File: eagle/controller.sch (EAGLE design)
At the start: 1 part, among them X1 FH12-18S-0.5SH

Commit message: schematics added
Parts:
- added IC1, IC2: ULN2003AD, uln-udn:ULN2003AD
- added JP1: (no value), pinhead:PINHD-1X7/90
- added JP2, JP3, JP4: (no value), pinhead:PINHD-1X2
- added JP5: (no value), pinhead:PINHD-1X5/90
- added U1: ARDUINO_PRO_MINI, Halley.rpt:ARDUINO_PRO_MINI
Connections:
- new net GND: IC1.GND, IC2.GND, JP2.1, JP3.1, JP4.1, JP5.1, U1.GND
- new net N$1: IC1.I1, U1.A0
- new net N$10: IC2.I3, U1.D10
- new net N$11: IC2.I4, U1.D11(MOSI)
- new net N$12: IC2.I5, U1.D12(MISO)
- new net N$13: JP5.5, U1.D4
- new net N$14: JP5.4, U1.D5
- new net N$15: JP5.3, U1.D6
- new net N$16: JP5.2, U1.D7
- new net N$17: JP3.2, U1.TXO(D0)
- new net N$18: JP2.2, U1.RXI(D1)
- new net N$19: IC2.I6, U1.A5
- new net N$2: IC1.I2, U1.A1
- new net N$20: IC1.O1, JP1.1
- new net N$21: IC1.O2, JP1.2
- new net N$22: IC1.O3, JP1.3
- new net N$23: IC1.O4, JP1.4
- new net N$24: IC1.O5, JP1.5
- new net N$25: IC1.O6, JP1.6
- new net N$26: IC1.O7, JP1.7
- new net N$3: IC1.I3, U1.A2
- new net N$4: IC1.I4, U1.A3
- new net N$5: IC1.I5, U1.D3
- new net N$6: IC1.I6, U1.A4
- new net N$7: IC1.I7, U1.D2
- new net N$8: IC2.I1, U1.D8
- new net N$9: IC2.I2, U1.D9
- new net V+: JP4.2, U1.RAW
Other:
- moved on the sheet: X1-1, X1-10, X1-11, X1-12, X1-13, X1-14, X1-15, X1-16, X1-17, X1-18, X1-2, X1-3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

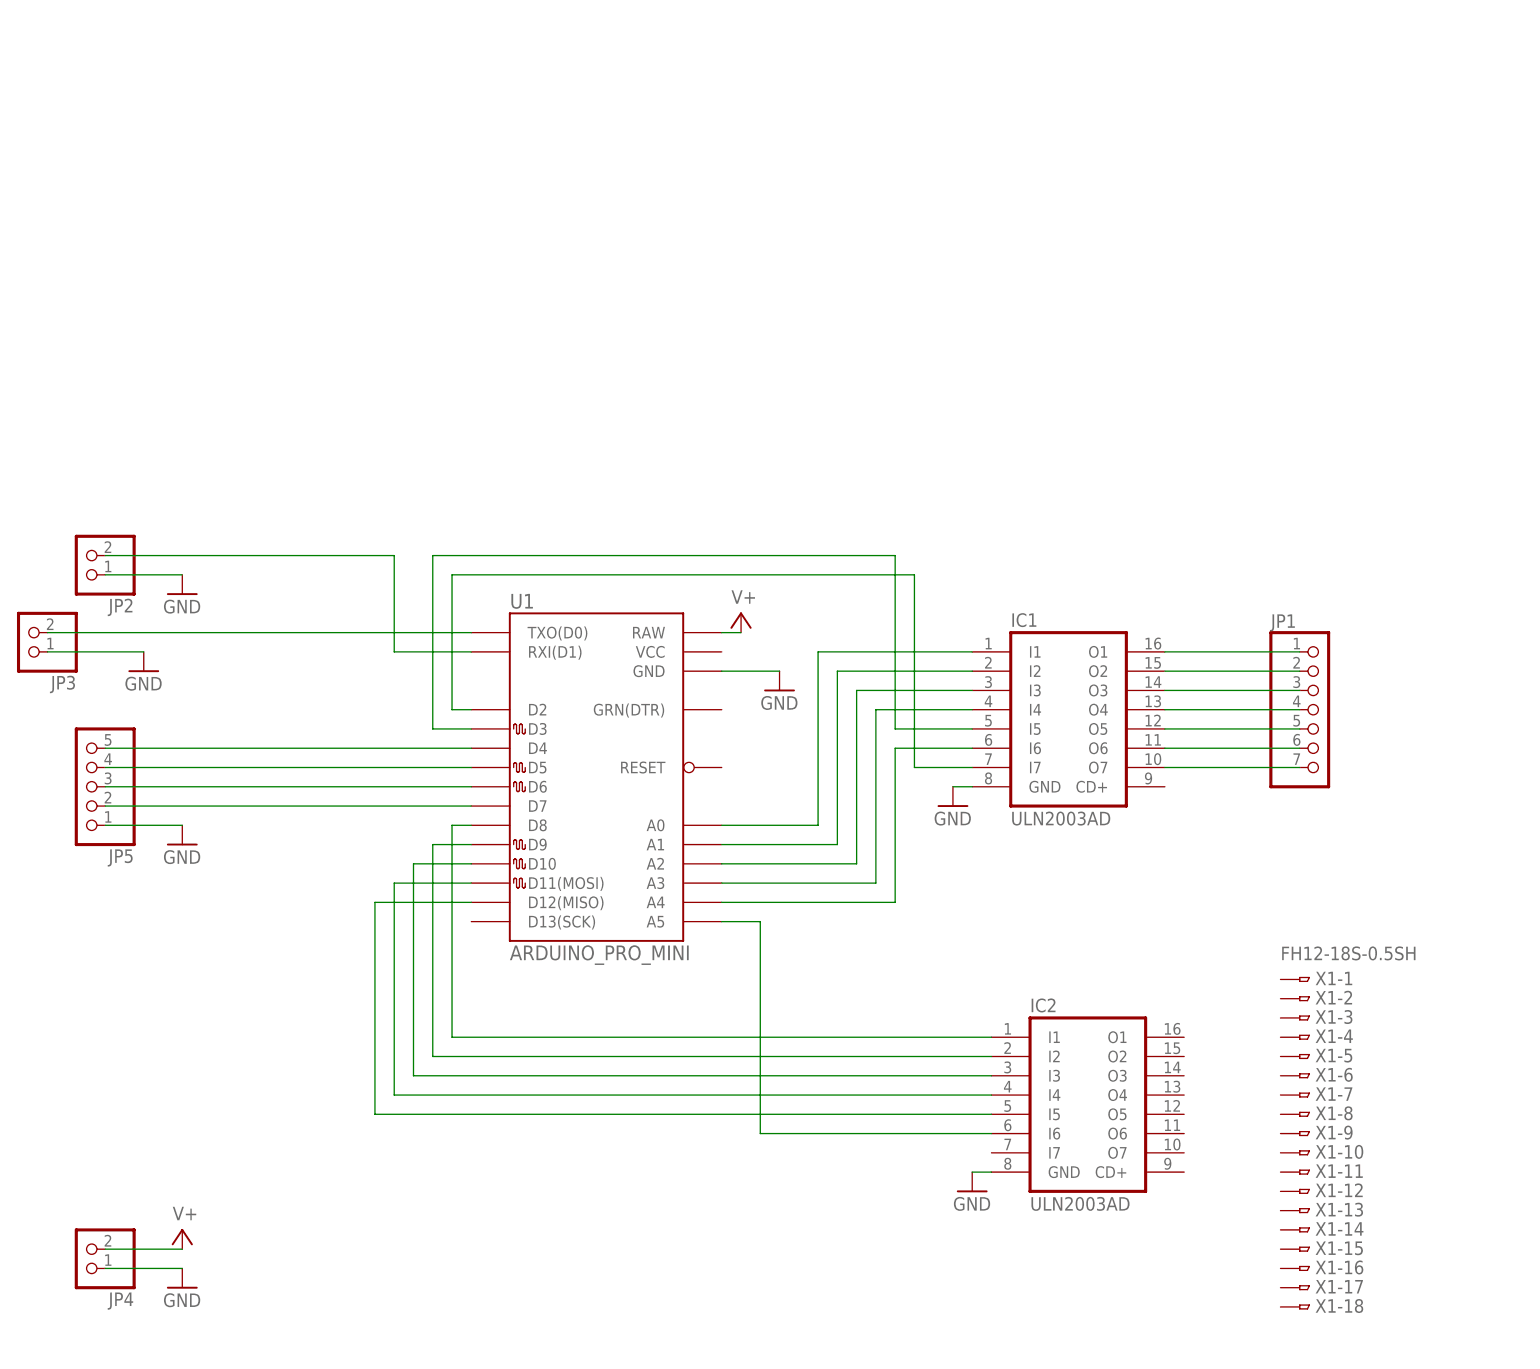
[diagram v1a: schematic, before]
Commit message: routed the board, updated bom
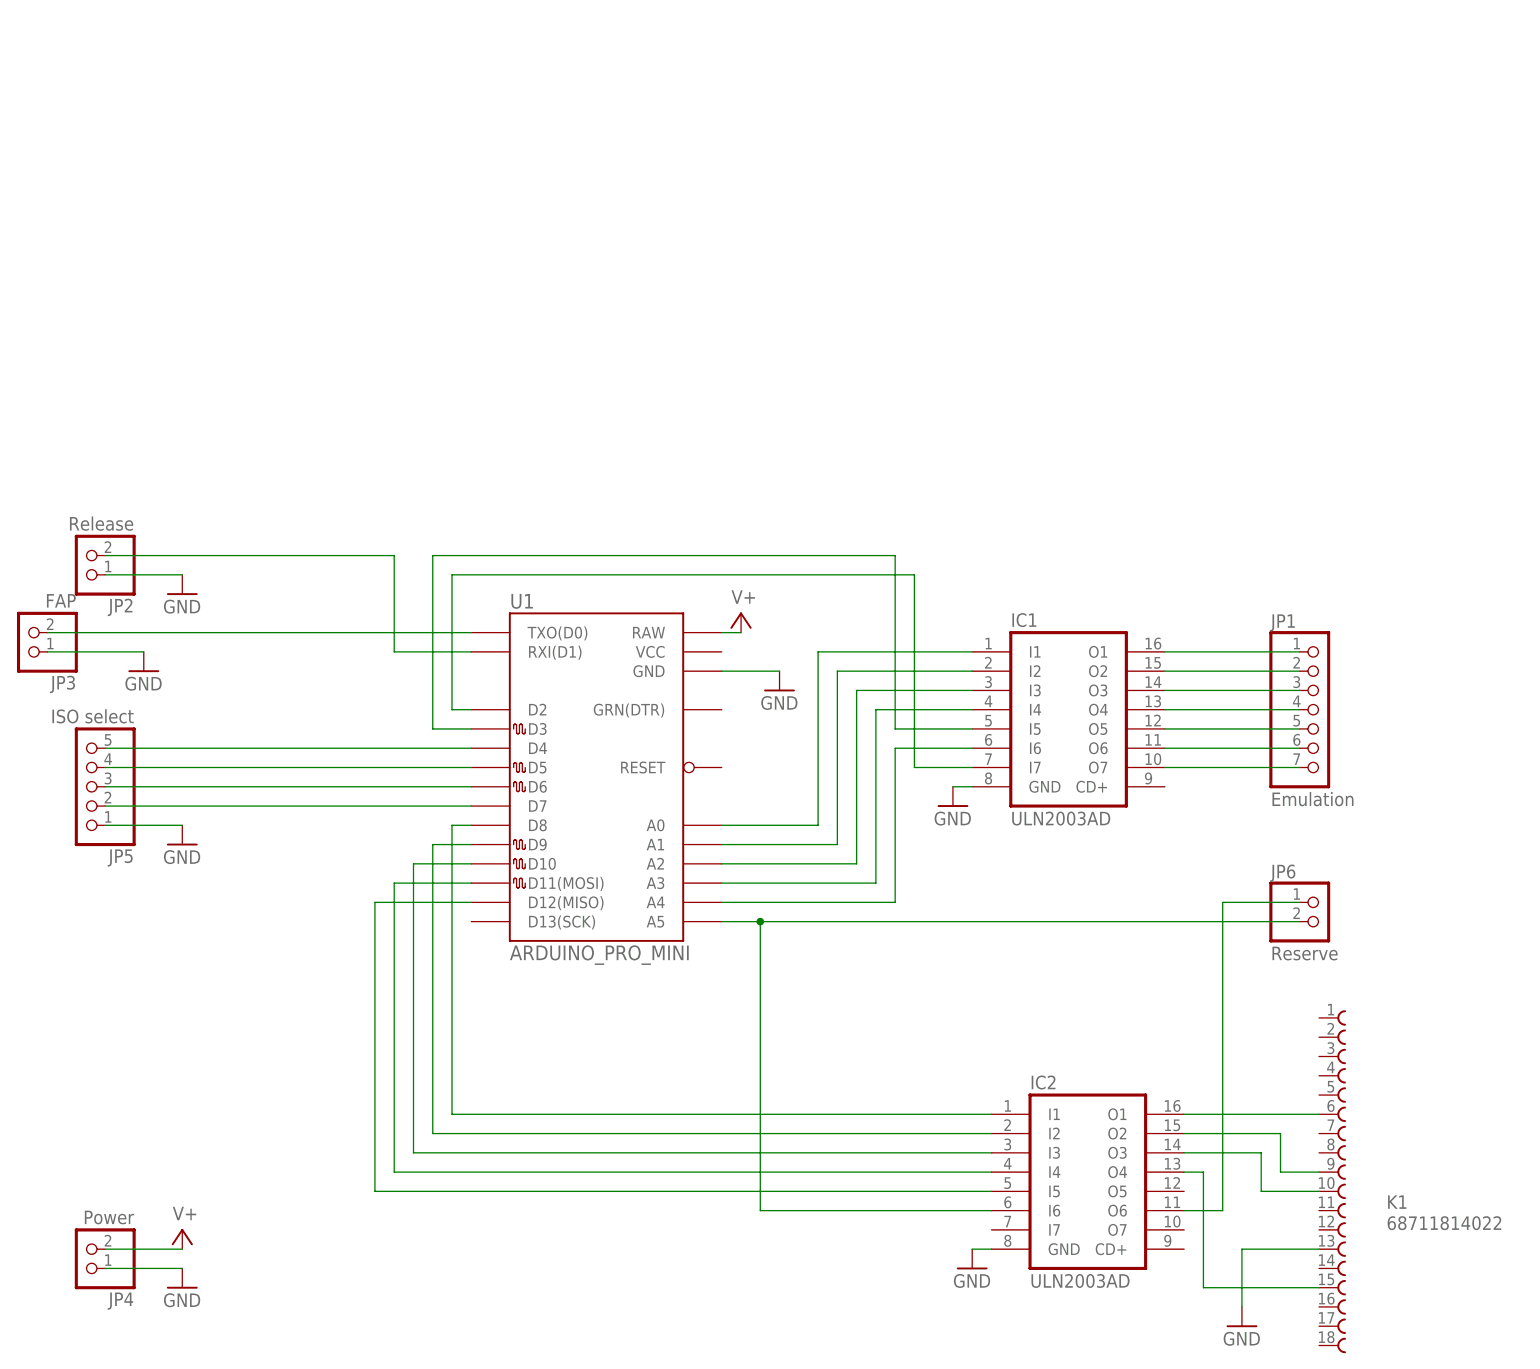
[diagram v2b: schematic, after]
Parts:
- removed X1: FH12-18S-0.5SH, con-hirose:FH12-18S-0.5SH
- added JP6: Reserve, pinhead:PINHD-1X2
- added K1: 68711814022, Wuerth_Elektronik_eiCan_03_ZIF_Connectors_Flat_Flexible_Cable:68711814022
- JP1: value (none) -> Emulation
- JP2: value (none) -> Release
- JP3: value (none) -> FAP
- JP4: value (none) -> Power
- JP5: value (none) -> ISO select
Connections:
- new net N$27: IC2.O6, JP6.1
- new net N$28: IC2.O1, K1.6
- new net N$29: IC2.O2, K1.9
- new net N$30: IC2.O3, K1.10
- new net N$31: IC2.O4, K1.15
- net GND: now also K1.13
- net N$19: now also JP6.2
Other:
- moved on the sheet: IC2
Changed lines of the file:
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@@
 </variantdefs>
 <classes>
-<class number="0" name="default" width="0" drill="0">
+<class number="0" name="default" width="0.2794" drill="0.381">
+<clearance class="0" value="0.1524"/>
 </class>
 </classes>
@@
 <part name="IC1" library="uln-udn" deviceset="ULN2003A" device="D"/>
 <part name="IC2" library="uln-udn" deviceset="ULN2003A" device="D"/>
-<part name="X1" library="con-hirose" deviceset="FH12-18S-0.5S" device="H"/>
 <part name="U1" library="Halley.rpt" deviceset="ARDUINO_PRO_MINI" device=""/>
 <part name="GND2" library="supply1" deviceset="GND" device=""/>
@@
 <part name="GND7" library="supply1" deviceset="GND" device=""/>
 <part name="GND1" library="supply1" deviceset="GND" device=""/>
-<part name="JP1" library="pinhead" deviceset="PINHD-1X7" device="/90"/>
-<part name="JP2" library="pinhead" deviceset="PINHD-1X2" device=""/>
-<part name="JP3" library="pinhead" deviceset="PINHD-1X2" device=""/>
-<part name="JP4" library="pinhead" deviceset="PINHD-1X2" device=""/>
-<part name="JP5" library="pinhead" deviceset="PINHD-1X5" device="/90"/>
+<part name="JP1" library="pinhead" deviceset="PINHD-1X7" device="/90" value="Emulation"/>
+<part name="JP2" library="pinhead" deviceset="PINHD-1X2" device="" value="Release"/>
+<part name="JP3" library="pinhead" deviceset="PINHD-1X2" device="" value="FAP"/>
+<part name="JP4" library="pinhead" deviceset="PINHD-1X2" device="" value="Power"/>
+<part name="JP5" library="pinhead" deviceset="PINHD-1X5" device="/90" value="ISO select"/>
+<part name="K1" library="Wuerth_Elektronik_eiCan_03_ZIF_Connectors_Flat_Flexible_Cable" deviceset="68711814022" device=""/>
+<part name="JP6" library="pinhead" deviceset="PINHD-1X2" device="" value="Reserve"/>
+<part name="GND8" library="supply1" deviceset="GND" device=""/>
 </parts>
 <sheets>
@@
 <instances>
 <instance part="IC1" gate="A" x="116.84" y="73.66"/>
-<instance part="IC2" gate="A" x="119.38" y="22.86"/>
-<instance part="X1" gate="-1" x="147.32" y="38.1"/>
-<instance part="X1" gate="-2" x="147.32" y="35.56"/>
-<instance part="X1" gate="-3" x="147.32" y="33.02"/>
-<instance part="X1" gate="-4" x="147.32" y="30.48"/>
-<instance part="X1" gate="-5" x="147.32" y="27.94"/>
-<instance part="X1" gate="-6" x="147.32" y="25.4"/>
-<instance part="X1" gate="-7" x="147.32" y="22.86"/>
-<instance part="X1" gate="-8" x="147.32" y="20.32"/>
-<instance part="X1" gate="-9" x="147.32" y="17.78"/>
-<instance part="X1" gate="-10" x="147.32" y="15.24"/>
-<instance part="X1" gate="-11" x="147.32" y="12.7"/>
-<instance part="X1" gate="-12" x="147.32" y="10.16"/>
-<instance part="X1" gate="-13" x="147.32" y="7.62"/>
-<instance part="X1" gate="-14" x="147.32" y="5.08"/>
-<instance part="X1" gate="-15" x="147.32" y="2.54"/>
-<instance part="X1" gate="-16" x="147.32" y="0"/>
-<instance part="X1" gate="-17" x="147.32" y="-2.54"/>
-<instance part="X1" gate="-18" x="147.32" y="-5.08"/>
+<instance part="IC2" gate="A" x="119.38" y="12.7"/>
 <instance part="U1" gate="G$1" x="53.34" y="63.5"/>
-<instance part="GND2" gate="1" x="104.14" y="10.16"/>
+<instance part="GND2" gate="1" x="104.14" y="0"/>
 <instance part="GND3" gate="1" x="101.6" y="60.96"/>
 <instance part="GND4" gate="1" x="0" y="55.88"/>
@@
 <instance part="JP4" gate="G$1" x="-12.7" y="2.54" rot="R180"/>
 <instance part="JP5" gate="A" x="-12.7" y="63.5" rot="R180"/>
+<instance part="K1" gate="G$1" x="154.94" y="7.62"/>
+<instance part="JP6" gate="G$1" x="149.86" y="45.72"/>
+<instance part="GND8" gate="1" x="139.7" y="-7.62"/>
 </instances>
 <busses>
@@
 <pinref part="IC2" gate="A" pin="GND"/>
 <pinref part="GND2" gate="1" pin="GND"/>
-<wire x1="104.14" y1="12.7" x2="106.68" y2="12.7" width="0.1524" layer="91"/>
+<wire x1="104.14" y1="2.54" x2="106.68" y2="2.54" width="0.1524" layer="91"/>
 </segment>
 <segment>
@@
 <wire x1="78.74" y1="78.74" x2="71.12" y2="78.74" width="0.1524" layer="91"/>
 </segment>
+<segment>
+<pinref part="K1" gate="G$1" pin="13"/>
+<pinref part="GND8" gate="1" pin="GND"/>
+<wire x1="149.86" y1="2.54" x2="139.7" y2="2.54" width="0.1524" layer="91"/>
+<wire x1="139.7" y1="2.54" x2="139.7" y2="-5.08" width="0.1524" layer="91"/>
+</segment>
 </net>
 <net name="N$8" class="0">
@@
 <pinref part="U1" gate="G$1" pin="D8"/>
 <wire x1="38.1" y1="58.42" x2="35.56" y2="58.42" width="0.1524" layer="91"/>
-<wire x1="35.56" y1="58.42" x2="35.56" y2="30.48" width="0.1524" layer="91"/>
+<wire x1="35.56" y1="58.42" x2="35.56" y2="20.32" width="0.1524" layer="91"/>
 <pinref part="IC2" gate="A" pin="I1"/>
-<wire x1="35.56" y1="30.48" x2="106.68" y2="30.48" width="0.1524" layer="91"/>
+<wire x1="35.56" y1="20.32" x2="106.68" y2="20.32" width="0.1524" layer="91"/>
 </segment>
 </net>
@@
 <pinref part="U1" gate="G$1" pin="D9"/>
 <wire x1="38.1" y1="55.88" x2="33.02" y2="55.88" width="0.1524" layer="91"/>
-<wire x1="33.02" y1="55.88" x2="33.02" y2="27.94" width="0.1524" layer="91"/>
+<wire x1="33.02" y1="55.88" x2="33.02" y2="17.78" width="0.1524" layer="91"/>
 <pinref part="IC2" gate="A" pin="I2"/>
-<wire x1="33.02" y1="27.94" x2="106.68" y2="27.94" width="0.1524" layer="91"/>
+<wire x1="33.02" y1="17.78" x2="106.68" y2="17.78" width="0.1524" layer="91"/>
 </segment>
 </net>
@@
 <segment>
 <pinref part="IC2" gate="A" pin="I3"/>
-<wire x1="106.68" y1="25.4" x2="30.48" y2="25.4" width="0.1524" layer="91"/>
-<wire x1="30.48" y1="25.4" x2="30.48" y2="53.34" width="0.1524" layer="91"/>
+<wire x1="106.68" y1="15.24" x2="30.48" y2="15.24" width="0.1524" layer="91"/>
+<wire x1="30.48" y1="15.24" x2="30.48" y2="53.34" width="0.1524" layer="91"/>
 <pinref part="U1" gate="G$1" pin="D10"/>
 <wire x1="30.48" y1="53.34" x2="38.1" y2="53.34" width="0.1524" layer="91"/>
@@
 <segment>
 <pinref part="IC2" gate="A" pin="I4"/>
-<wire x1="106.68" y1="22.86" x2="27.94" y2="22.86" width="0.1524" layer="91"/>
-<wire x1="27.94" y1="22.86" x2="27.94" y2="50.8" width="0.1524" layer="91"/>
+<wire x1="106.68" y1="12.7" x2="27.94" y2="12.7" width="0.1524" layer="91"/>
+<wire x1="27.94" y1="12.7" x2="27.94" y2="50.8" width="0.1524" layer="91"/>
 <pinref part="U1" gate="G$1" pin="D11(MOSI)"/>
 <wire x1="27.94" y1="50.8" x2="38.1" y2="50.8" width="0.1524" layer="91"/>
@@
 <segment>
 <pinref part="IC2" gate="A" pin="I5"/>
-<wire x1="106.68" y1="20.32" x2="25.4" y2="20.32" width="0.1524" layer="91"/>
-<wire x1="25.4" y1="20.32" x2="25.4" y2="48.26" width="0.1524" layer="91"/>
+<wire x1="106.68" y1="10.16" x2="25.4" y2="10.16" width="0.1524" layer="91"/>
+<wire x1="25.4" y1="10.16" x2="25.4" y2="48.26" width="0.1524" layer="91"/>
 <pinref part="U1" gate="G$1" pin="D12(MISO)"/>
 <wire x1="25.4" y1="48.26" x2="38.1" y2="48.26" width="0.1524" layer="91"/>
@@
 <pinref part="U1" gate="G$1" pin="A5"/>
 <wire x1="71.12" y1="45.72" x2="76.2" y2="45.72" width="0.1524" layer="91"/>
-<wire x1="76.2" y1="45.72" x2="76.2" y2="17.78" width="0.1524" layer="91"/>
+<wire x1="76.2" y1="45.72" x2="76.2" y2="7.62" width="0.1524" layer="91"/>
 <pinref part="IC2" gate="A" pin="I6"/>
-<wire x1="76.2" y1="17.78" x2="106.68" y2="17.78" width="0.1524" layer="91"/>
+<wire x1="76.2" y1="7.62" x2="106.68" y2="7.62" width="0.1524" layer="91"/>
+<pinref part="JP6" gate="G$1" pin="2"/>
+<wire x1="76.2" y1="45.72" x2="147.32" y2="45.72" width="0.1524" layer="91"/>
+<junction x="76.2" y="45.72"/>
 </segment>
 </net>
@@
 </segment>
 </net>
+<net name="N$27" class="0">
+<segment>
+<pinref part="IC2" gate="A" pin="O6"/>
+<wire x1="132.08" y1="7.62" x2="137.16" y2="7.62" width="0.1524" layer="91"/>
+<wire x1="137.16" y1="7.62" x2="137.16" y2="48.26" width="0.1524" layer="91"/>
+<pinref part="JP6" gate="G$1" pin="1"/>
+<wire x1="137.16" y1="48.26" x2="147.32" y2="48.26" width="0.1524" layer="91"/>
+</segment>
+</net>
+<net name="N$28" class="0">
+<segment>
+<pinref part="IC2" gate="A" pin="O1"/>
+<pinref part="K1" gate="G$1" pin="6"/>
+<wire x1="132.08" y1="20.32" x2="149.86" y2="20.32" width="0.1524" layer="91"/>
+</segment>
+</net>
+<net name="N$29" class="0">
+<segment>
+<pinref part="IC2" gate="A" pin="O2"/>
+<wire x1="132.08" y1="17.78" x2="144.78" y2="17.78" width="0.1524" layer="91"/>
+<wire x1="144.78" y1="17.78" x2="144.78" y2="12.7" width="0.1524" layer="91"/>
+<pinref part="K1" gate="G$1" pin="9"/>
+<wire x1="144.78" y1="12.7" x2="149.86" y2="12.7" width="0.1524" layer="91"/>
+</segment>
+</net>
+<net name="N$30" class="0">
+<segment>
+<pinref part="IC2" gate="A" pin="O3"/>
+<wire x1="132.08" y1="15.24" x2="142.24" y2="15.24" width="0.1524" layer="91"/>
+<wire x1="142.24" y1="15.24" x2="142.24" y2="10.16" width="0.1524" layer="91"/>
+<pinref part="K1" gate="G$1" pin="10"/>
+<wire x1="142.24" y1="10.16" x2="149.86" y2="10.16" width="0.1524" layer="91"/>
+</segment>
+</net>
+<net name="N$31" class="0">
+<segment>
+<pinref part="IC2" gate="A" pin="O4"/>
+<wire x1="132.08" y1="12.7" x2="134.62" y2="12.7" width="0.1524" layer="91"/>
+<wire x1="134.62" y1="12.7" x2="134.62" y2="-2.54" width="0.1524" layer="91"/>
+<pinref part="K1" gate="G$1" pin="15"/>
+<wire x1="134.62" y1="-2.54" x2="149.86" y2="-2.54" width="0.1524" layer="91"/>
+</segment>
+</net>

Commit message: production board REVA
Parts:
- JP6: device pinhead:PINHD-1X2 -> pinhead:PINHD-1X3
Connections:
- new net N$32: IC2.O5, JP6.3
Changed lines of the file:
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@@
 <part name="JP5" library="pinhead" deviceset="PINHD-1X5" device="/90" value="ISO select"/>
 <part name="K1" library="Wuerth_Elektronik_eiCan_03_ZIF_Connectors_Flat_Flexible_Cable" deviceset="68711814022" device=""/>
-<part name="JP6" library="pinhead" deviceset="PINHD-1X2" device="" value="Reserve"/>
 <part name="GND8" library="supply1" deviceset="GND" device=""/>
+<part name="JP6" library="pinhead" deviceset="PINHD-1X3" device="" value="Reserve"/>
 </parts>
 <sheets>
@@
 <instance part="JP5" gate="A" x="-12.7" y="63.5" rot="R180"/>
 <instance part="K1" gate="G$1" x="154.94" y="7.62"/>
-<instance part="JP6" gate="G$1" x="149.86" y="45.72"/>
 <instance part="GND8" gate="1" x="139.7" y="-7.62"/>
+<instance part="JP6" gate="A" x="149.86" y="45.72"/>
 </instances>
 <busses>
@@
 <pinref part="IC2" gate="A" pin="I6"/>
 <wire x1="76.2" y1="7.62" x2="106.68" y2="7.62" width="0.1524" layer="91"/>
-<pinref part="JP6" gate="G$1" pin="2"/>
 <wire x1="76.2" y1="45.72" x2="147.32" y2="45.72" width="0.1524" layer="91"/>
 <junction x="76.2" y="45.72"/>
+<pinref part="JP6" gate="A" pin="2"/>
 </segment>
 </net>
@@
 <wire x1="132.08" y1="7.62" x2="137.16" y2="7.62" width="0.1524" layer="91"/>
 <wire x1="137.16" y1="7.62" x2="137.16" y2="48.26" width="0.1524" layer="91"/>
-<pinref part="JP6" gate="G$1" pin="1"/>
 <wire x1="137.16" y1="48.26" x2="147.32" y2="48.26" width="0.1524" layer="91"/>
+<pinref part="JP6" gate="A" pin="1"/>
 </segment>
 </net>
@@
 </segment>
 </net>
+<net name="N$32" class="0">
+<segment>
+<pinref part="IC2" gate="A" pin="O5"/>
+<wire x1="132.08" y1="10.16" x2="139.7" y2="10.16" width="0.1524" layer="91"/>
+<wire x1="139.7" y1="10.16" x2="139.7" y2="43.18" width="0.1524" layer="91"/>
+<pinref part="JP6" gate="A" pin="3"/>
+<wire x1="139.7" y1="43.18" x2="147.32" y2="43.18" width="0.1524" layer="91"/>
+</segment>
+</net>
